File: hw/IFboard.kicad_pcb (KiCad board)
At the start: 2 copper layers, 60 x 65.1 mm, 67 parts, among them J1 USB_C_Receptacle_USB2.0_16P, J2 Conn_01x02_Socket, J3 Conn_ARM_SWD_TagConnect_TC203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, J4 Conn_01x02_Socket, J5 Conn_01x02_Socket, J6 Conn_01x02_Socket, SW3 SW_Push, SW4 SW_Push, SW5 SW_Push, SW6 SW_Push, U2 XC6206PxxxMR, U3 TCAN3413DR, U4 ST4E1240DT, U5 MAX232ESE+T, U6 STM32G0B1CBTx

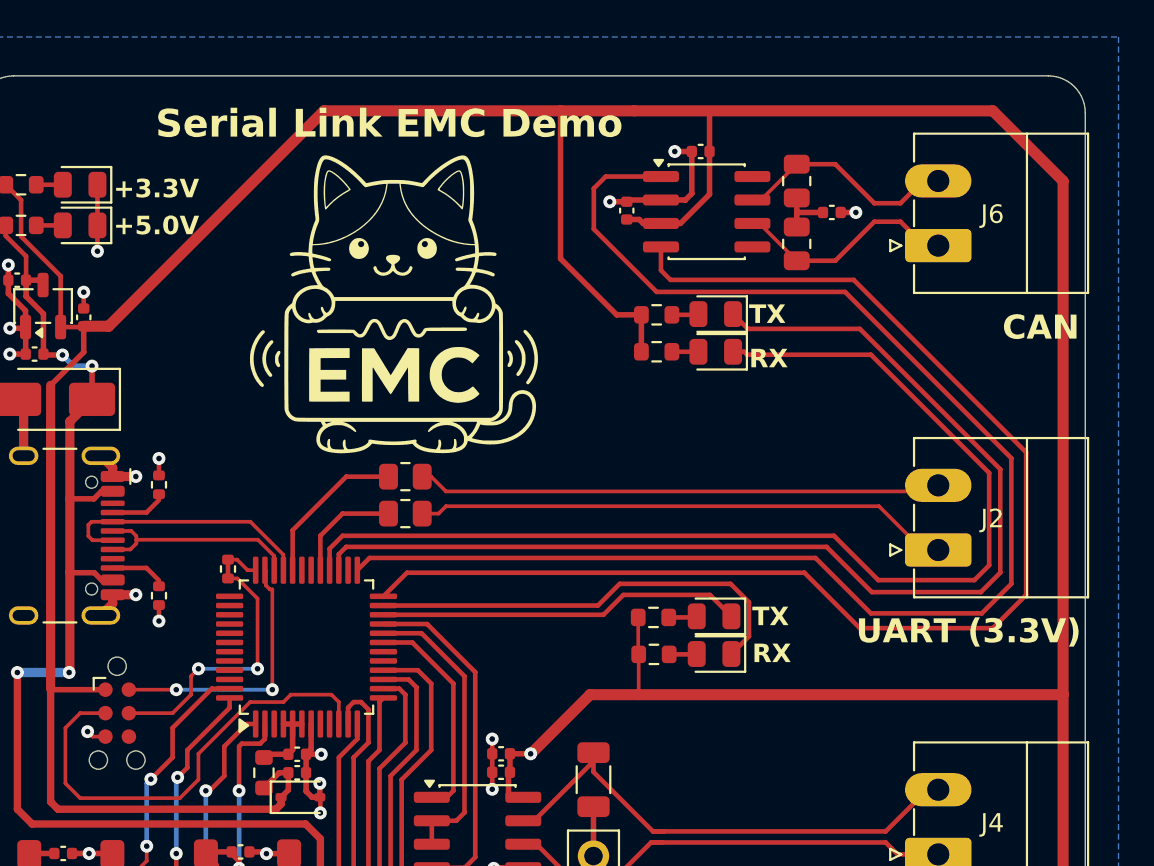
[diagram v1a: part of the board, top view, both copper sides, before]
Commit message: wip:add small display
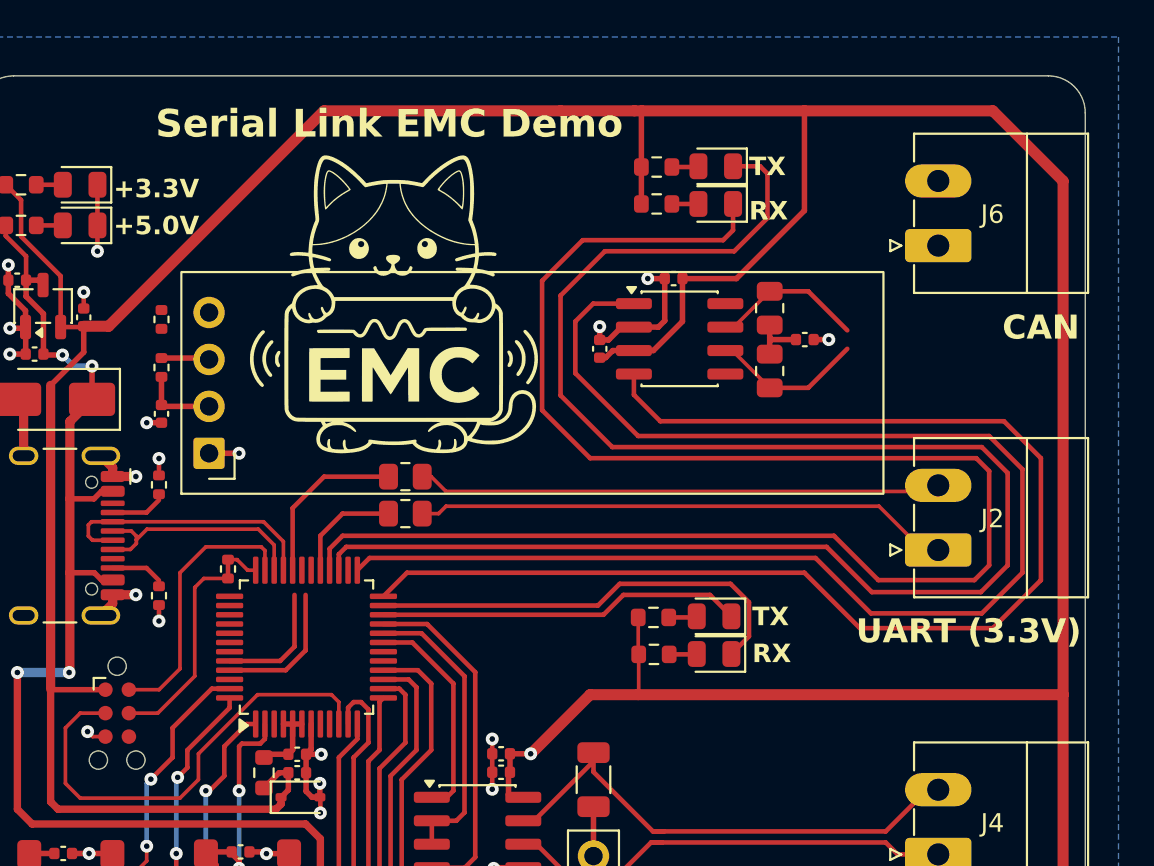
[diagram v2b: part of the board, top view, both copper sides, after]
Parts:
- added C23: 1u, Capacitor_SMD:C_0402_1005Metric, F.Cu at (60.9, 68.6)
- added R20: 5.1k, Resistor_SMD:R_0402_1005Metric, F.Cu at (60.9, 66.1)
- added R21: 5.1k, Resistor_SMD:R_0402_1005Metric, F.Cu at (60.9, 63.5)
- added U7: ER_OLEDM0.91_1x-I2C, Display:ER_OLEDM0.91_1x-I2C, F.Cu at (63.5, 70.8)
- moved D5 8.00 mm to (90.9, 55.2)
- moved R11 8.00 mm to (87.7, 55.3)
- moved D4 8.00 mm to (90.9, 57.3)
- moved R10 8.00 mm to (87.7, 57.3)
- moved C19 7.62 mm to (84.6, 65.1)
- moved R14 7.03 mm to (93.8, 62.9)
- moved R15 7.03 mm to (93.8, 66.3)
- moved C20 7.03 mm to (95.7, 64.6)
- moved C21 7.03 mm to (88.6, 61.3)
- moved U3 7.03 mm to (89.0, 64.6)
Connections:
- U6 pad 44: unconnected-(U6-PB5-Pad44) -> /SDA
- U6 pad 45: unconnected-(U6-PB6-Pad45) -> /SCL
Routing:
- net /CAN_RX_LED: track 61.8 -> 92.6 mm
- net /CAN_TX_LED: track 60.1 -> 89.0 mm
- net /SCL: track 0.00 -> 10.2 mm
- net /SDA: track 0.00 -> 6.63 mm
- net +3.3V: track 287.8 -> 292.8 mm
- net Net-(J6-Pin_1): track 12.3 -> 8.31 mm
- net Net-(J6-Pin_2): track 12.2 -> 8.28 mm
- net /SWCLK: track 14.4 -> 11.2 mm, vias 2 -> 0
- net GND: track 79.2 -> 81.8 mm, vias 30 -> 32
- net /FDCAN2_TX: track 78.2 -> 76.8 mm
- net /USB_D+: track 11.8 -> 12.6 mm
- net /USART1_RX: track 8.55 -> 9.26 mm
- net /FDCAN2_RX: track 70.1 -> 69.6 mm
- net /SWDIO: track 14.5 -> 14.8 mm, vias 2 -> 0

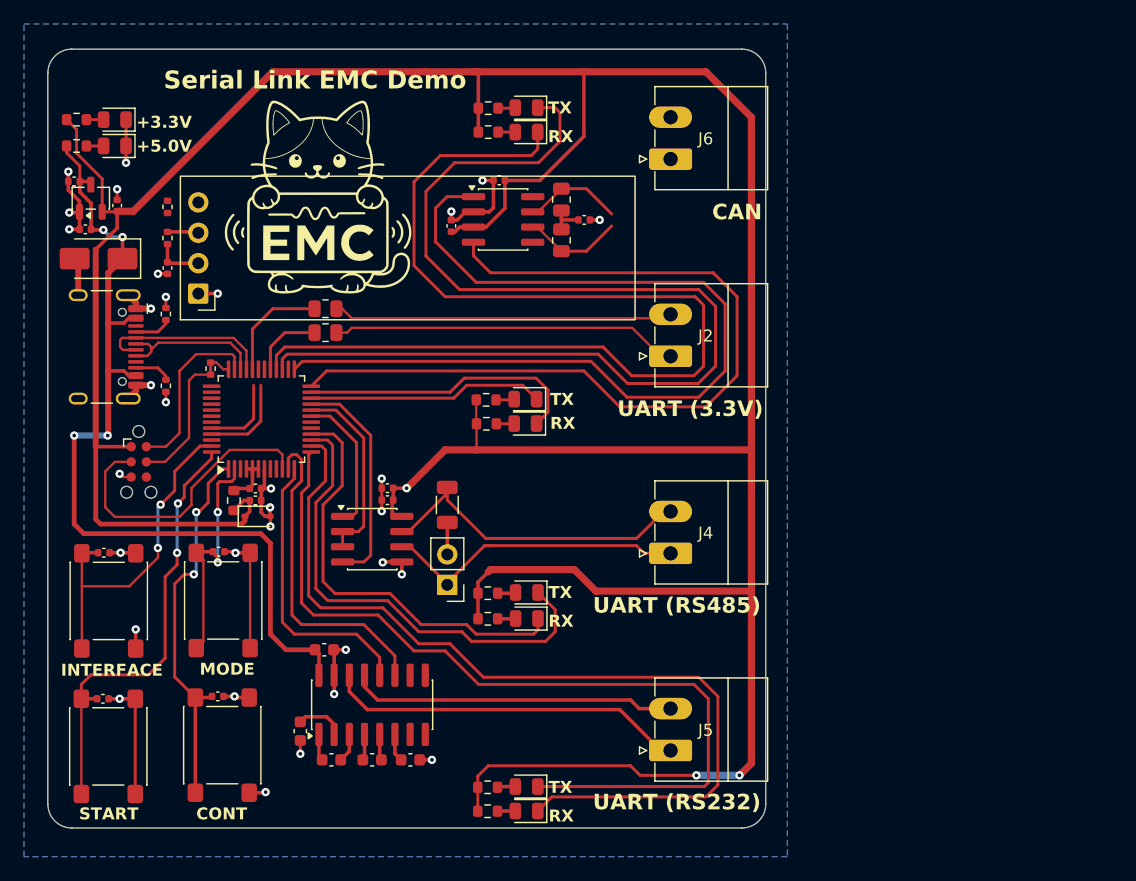
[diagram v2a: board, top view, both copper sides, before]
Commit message: display I2C connection done. not proud of it =)
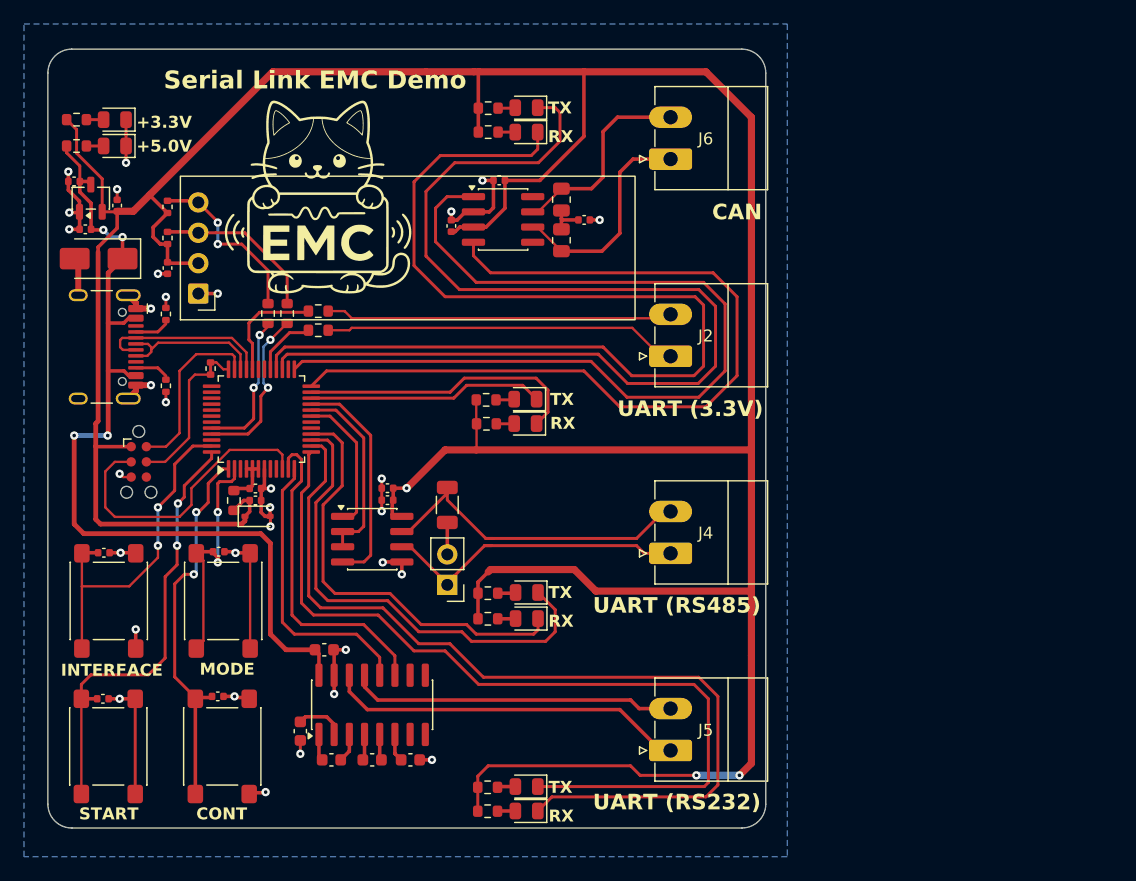
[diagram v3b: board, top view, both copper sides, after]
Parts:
- added G***: LOGO, LOGO, B.Cu at (73.5, 62.6)
- added R22: 0, Resistor_SMD:R_0603_1608Metric, F.Cu at (69.3, 72.4)
- added R23: 0, Resistor_SMD:R_0603_1608Metric, F.Cu at (70.9, 72.4)
- R7, R8: value 10 -> 0; footprint Resistor_SMD:R_0805_2012Metric -> Resistor_SMD:R_0603_1608Metric
- moved R7 0.63 mm to (73.5, 73.8)
- moved R8 0.63 mm to (73.5, 72.2)
- moved SW6 0.11 mm to (65.5, 108.6)
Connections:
- U6 pad 44: /SDA -> Net-(U6-PB5)
- U6 pad 45: /SCL -> Net-(U6-PB6)
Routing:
- net Net-(U6-PB6): track 0.00 -> 13.9 mm, vias 0 -> 2
- net Net-(U6-PB5): track 0.00 -> 12.3 mm, vias 0 -> 2
- net Net-(J6-Pin_1): track 8.31 -> 18.5 mm
- net Net-(J6-Pin_2): track 8.28 -> 17.0 mm
- net /SDA: track 6.63 -> 14.7 mm, vias 0 -> 2
- net +3.3V: track 292.8 -> 298.9 mm
- net /SCL: track 10.2 -> 13.9 mm
- net /USART1_TX: track 6.05 -> 5.38 mm
- net Net-(J2-Pin_2): track 28.5 -> 29.1 mm
- net Net-(J2-Pin_1): track 29.1 -> 29.7 mm
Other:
- board text added: "Thomas Shuttleworth (4BHEL) Leo Rexeis (4BHEL) Franz Patz HTL Graz-Gösting May 2026"
- board text removed: "Franz Patz HTL Graz-Gösting May 2026"

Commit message: forgot last time
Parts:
- J6: value Conn_01x02_Socket -> Conn_01x03_Socket; footprint Connector_Phoenix_MC:PhoenixContact_MC_1,5_2-G-3.5_1x02_P3.50mm_Horizontal -> Connector_Phoenix_MC:PhoenixContact_MC_1,5_3-G-3.5_1x03_P3.50mm_Horizontal
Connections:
- J6 pad 1: Net-(J6-Pin_1) -> unconnected-(J6-Pin_1-Pad1)
- R14 pad 1: Net-(J6-Pin_2) -> Net-(J6-Pin_3)
- R15 pad 2: Net-(J6-Pin_1) -> Net-(J6-Pin_2)
- U3 pad 6: Net-(J6-Pin_1) -> Net-(J6-Pin_2)
- U3 pad 7: Net-(J6-Pin_2) -> Net-(J6-Pin_3)
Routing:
- net Net-(J6-Pin_2): track 17.0 -> 35.6 mm
- net Net-(J6-Pin_1): track 18.5 -> 0.00 mm
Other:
- board size 60 x 65.1 mm -> 65 x 65.1 mm

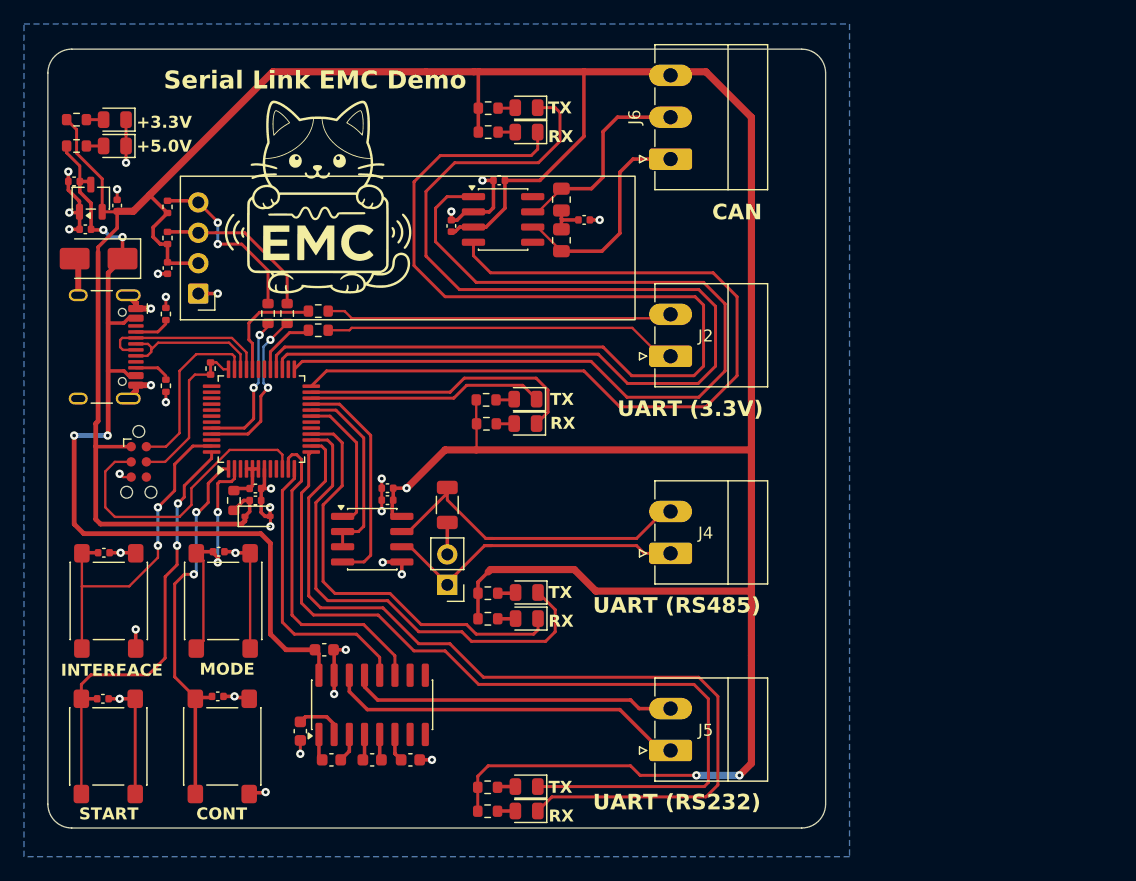
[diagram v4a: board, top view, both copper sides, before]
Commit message: tag:3.5mm connectors
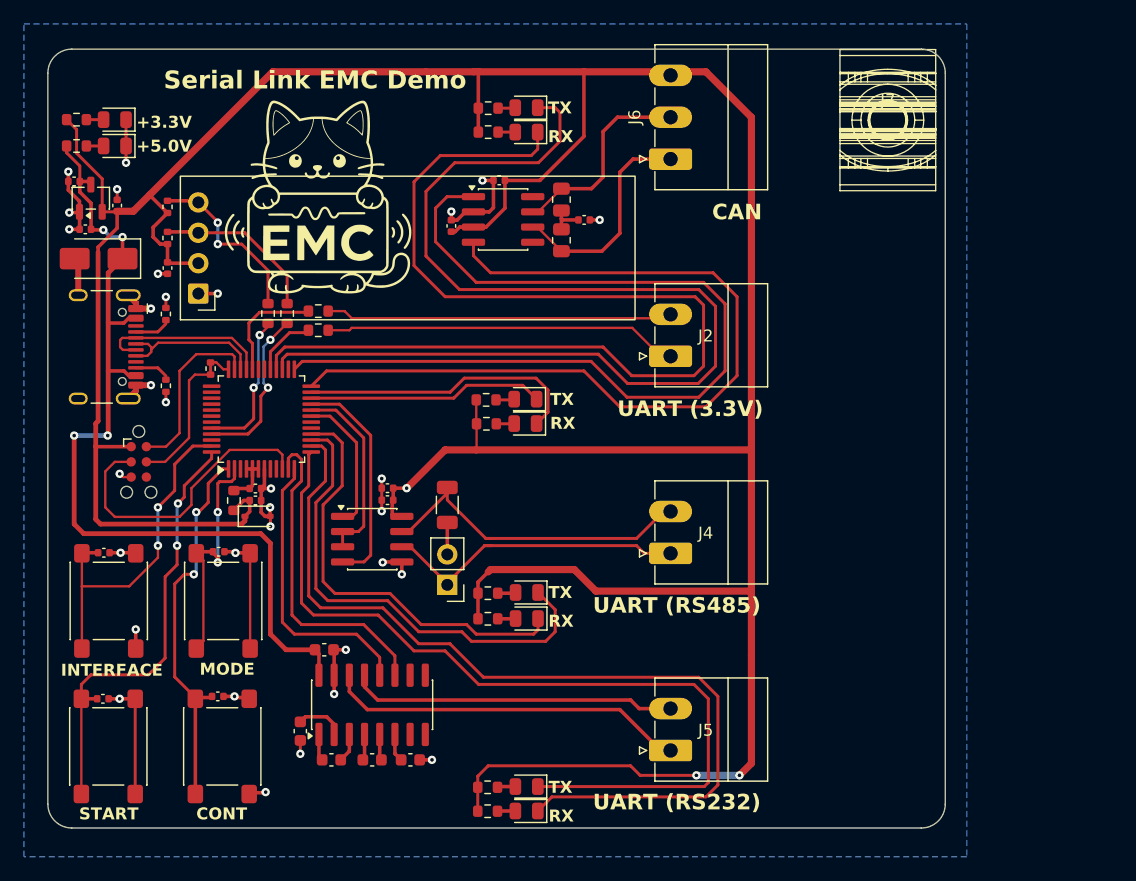
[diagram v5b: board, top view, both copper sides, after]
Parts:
- added J7: Conn_01x01_MountingPin, Connector_PinHeader_1.00mm:PinHeader_1x01_P1.00mm_Vertical, F.Cu at (121.1, 56.2)
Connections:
- J6 pad 1: unconnected-(J6-Pin_1-Pad1) -> GND
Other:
- board size 65 x 65.1 mm -> 75 x 65.1 mm

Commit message: wip
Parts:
- J2, J4, J5: value Conn_01x02_Socket -> Conn_01x03_Socket; footprint Connector_Phoenix_MC:PhoenixContact_MC_1,5_2-G-3.5_1x02_P3.50mm_Horizontal -> PZL:1881451
- moved J2 1.40 mm to (103.0, 77.4)
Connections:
- J6 pad 1: GND -> Net-(J6-Pin_1)
- J6 pad 3: Net-(J6-Pin_3) -> GND
- R14 pad 1: Net-(J6-Pin_3) -> Net-(J6-Pin_2)
- R15 pad 2: Net-(J6-Pin_2) -> Net-(J6-Pin_1)
- U3 pad 6: Net-(J6-Pin_2) -> Net-(J6-Pin_1)
- U3 pad 7: Net-(J6-Pin_3) -> Net-(J6-Pin_2)
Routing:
- net Net-(J6-Pin_2): track 35.6 -> 17.0 mm
- net Net-(J6-Pin_1): track 0.00 -> 18.5 mm
- net /FDCAN2_RX: track 69.6 -> 72.6 mm
- net /FDCAN2_TX: track 76.8 -> 79.4 mm
- net /CAN_RX_LED: track 92.6 -> 95.0 mm
- net /CAN_TX_LED: track 89.0 -> 91.3 mm
- net Net-(J2-Pin_2): track 29.1 -> 29.7 mm
- net Net-(J2-Pin_1): track 29.7 -> 30.3 mm
- net /USART4_RX_LED: track 71.7 -> 72.2 mm
- net /USART4_TX_LED: track 75.1 -> 75.7 mm

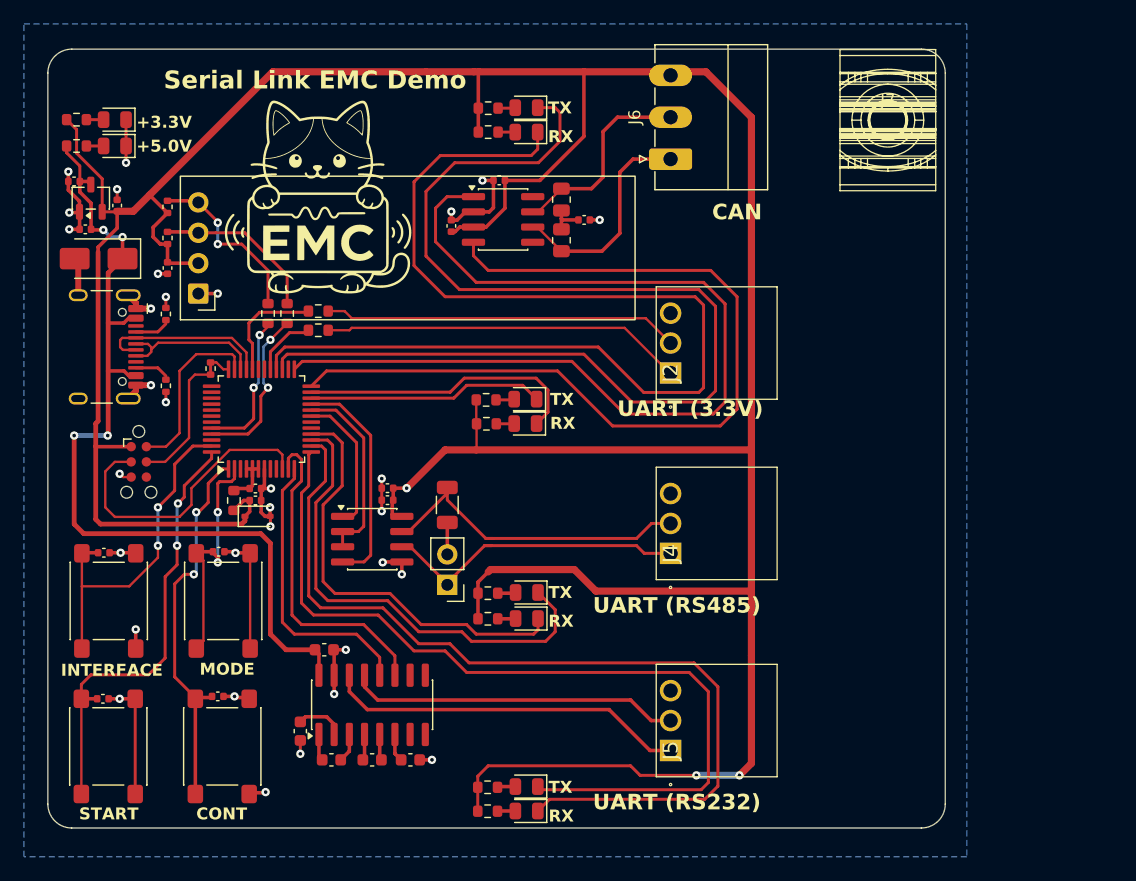
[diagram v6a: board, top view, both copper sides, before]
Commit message: swapped poition of two connectors for better routing
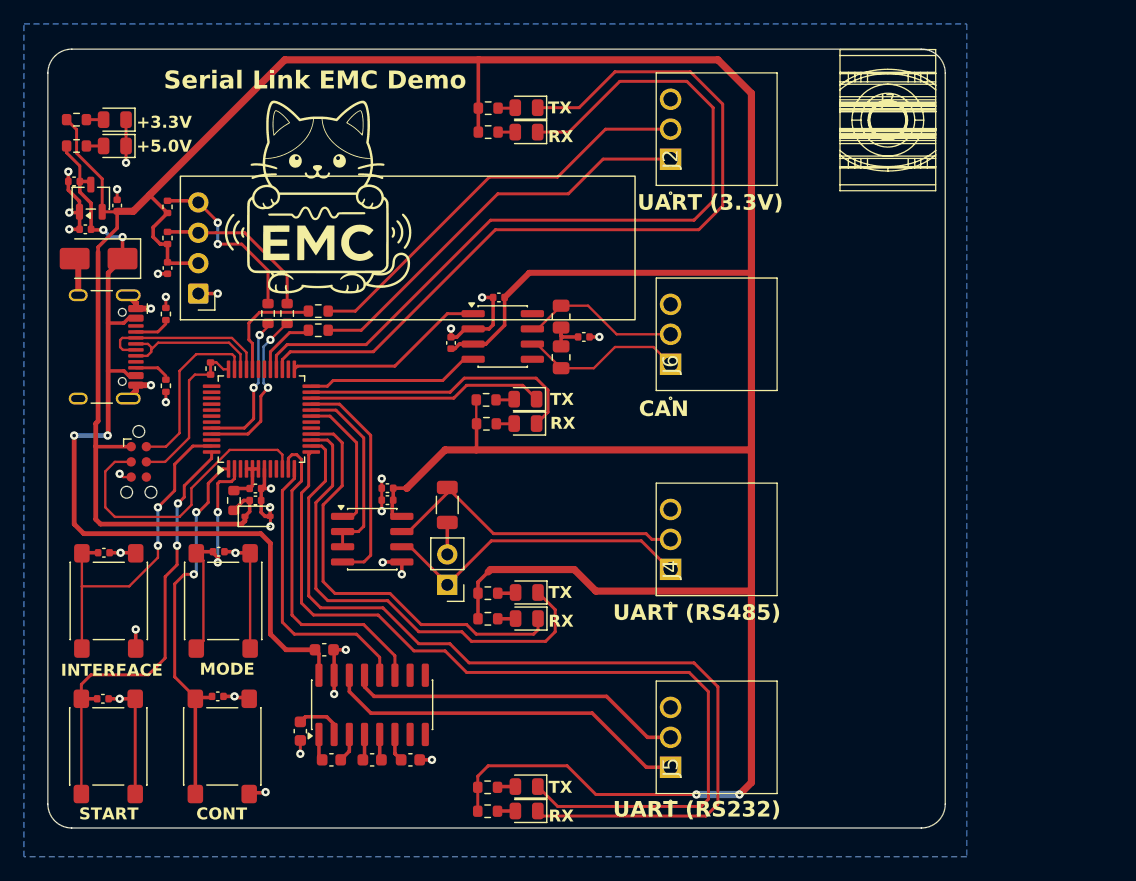
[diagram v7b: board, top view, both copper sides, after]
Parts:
- J6: footprint Connector_Phoenix_MC:PhoenixContact_MC_1,5_3-G-3.5_1x03_P3.50mm_Horizontal -> PZL:1881451
- moved J2 17.9 mm to (103.0, 59.5)
- moved J6 17.1 mm to (103.0, 76.7)
- moved C19 9.78 mm to (84.6, 74.9)
- moved C20 9.78 mm to (95.7, 74.4)
- moved U3 9.78 mm to (88.9, 74.3)
- moved R14 9.78 mm to (93.8, 72.7)
- moved C21 9.78 mm to (88.6, 71.1)
- moved R15 9.78 mm to (93.8, 76.1)
- moved J5 1.40 mm to (103.0, 110.3)
- moved J4 1.33 mm to (103.0, 93.8)
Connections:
- D4 pad 1: /CAN_TX_LED -> /USART1_TX_LED
- D5 pad 1: /CAN_RX_LED -> /USART1_RX_LED
- D6 pad 1: /USART1_TX_LED -> /CAN_TX_LED
- D8 pad 1: /USART1_RX_LED -> /CAN_RX_LED
- U6 pad 22: /USART1_RX_LED -> /CAN_RX_LED
- U6 pad 23: /USART1_TX_LED -> /CAN_TX_LED
- U6 pad 27: /CAN_RX_LED -> /USART1_RX_LED
- U6 pad 28: /CAN_TX_LED -> /USART1_TX_LED
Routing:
- net /CAN_RX_LED: track 95.0 -> 19.8 mm
- net /CAN_TX_LED: track 91.3 -> 23.9 mm
- net /FDCAN2_TX: track 79.4 -> 16.9 mm
- net /FDCAN2_RX: track 72.6 -> 14.5 mm
- net /USART1_RX_LED: track 19.8 -> 69.3 mm
- net /USART1_TX_LED: track 23.9 -> 68.1 mm
- net +3.3V: track 298.9 -> 312.0 mm, vias 3 -> 2
- net Net-(J2-Pin_2): track 29.7 -> 34.9 mm
- net Net-(J6-Pin_1): track 18.5 -> 13.7 mm
- net Net-(J2-Pin_1): track 30.3 -> 34.5 mm
- net Net-(J6-Pin_2): track 17.0 -> 13.3 mm
- net /USART4_RX_LED: track 72.2 -> 74.2 mm
- net Net-(J4-Pin_2): track 27.8 -> 26.1 mm
- net /USART4_TX_LED: track 75.7 -> 76.9 mm
- net /USART4_TX_MAX: track 30.3 -> 31.1 mm
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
